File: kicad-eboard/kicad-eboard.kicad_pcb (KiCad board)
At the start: 2 copper layers, 91 parts, among them J1 Conn_01x02, J19 Conn_01x10, SW10 AMT10_Encoder, SW4 LIMIT_1, SW5 LIMIT_2, SW6 AMT10_Encoder, SW7 AMT10_Encoder, SW8 AMT10_Encoder, SW9 AMT10_Encoder, U1 TinkerBoard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

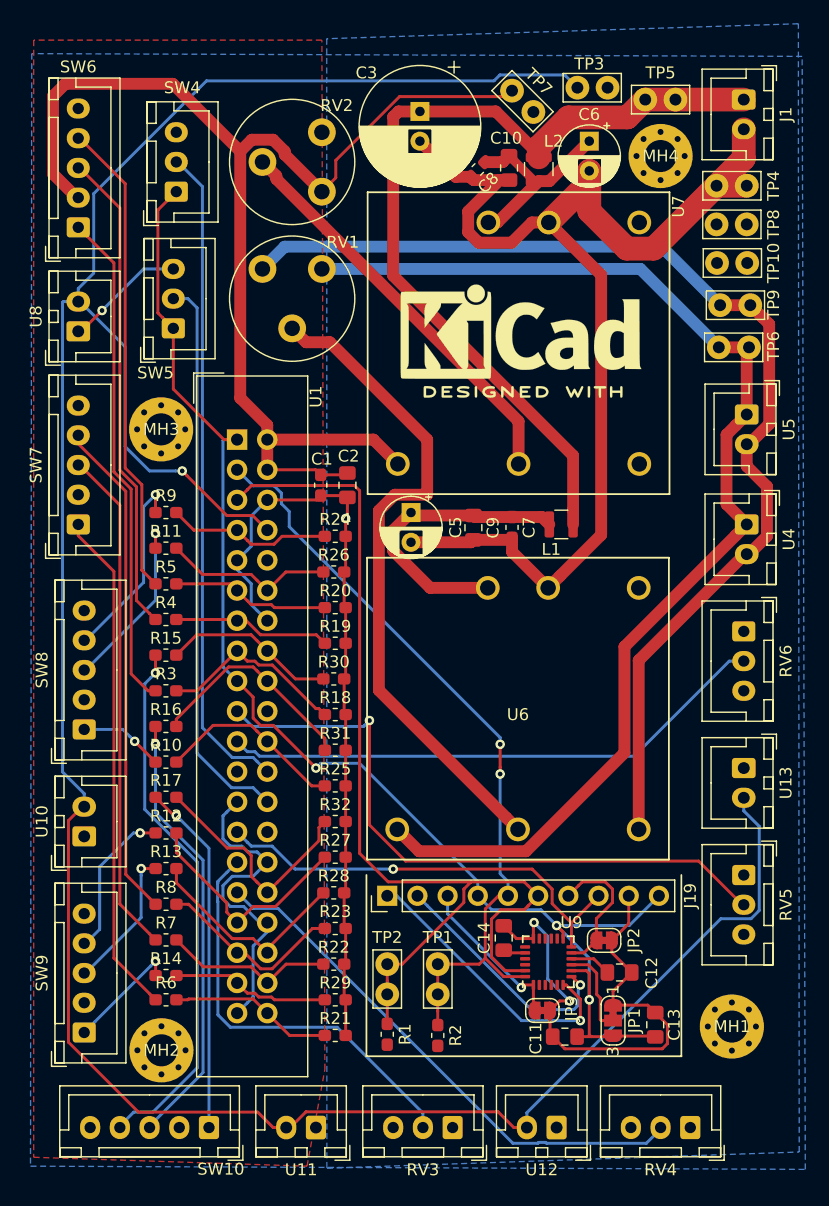
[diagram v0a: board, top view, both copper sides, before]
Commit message: Fix broken 3v3 pour
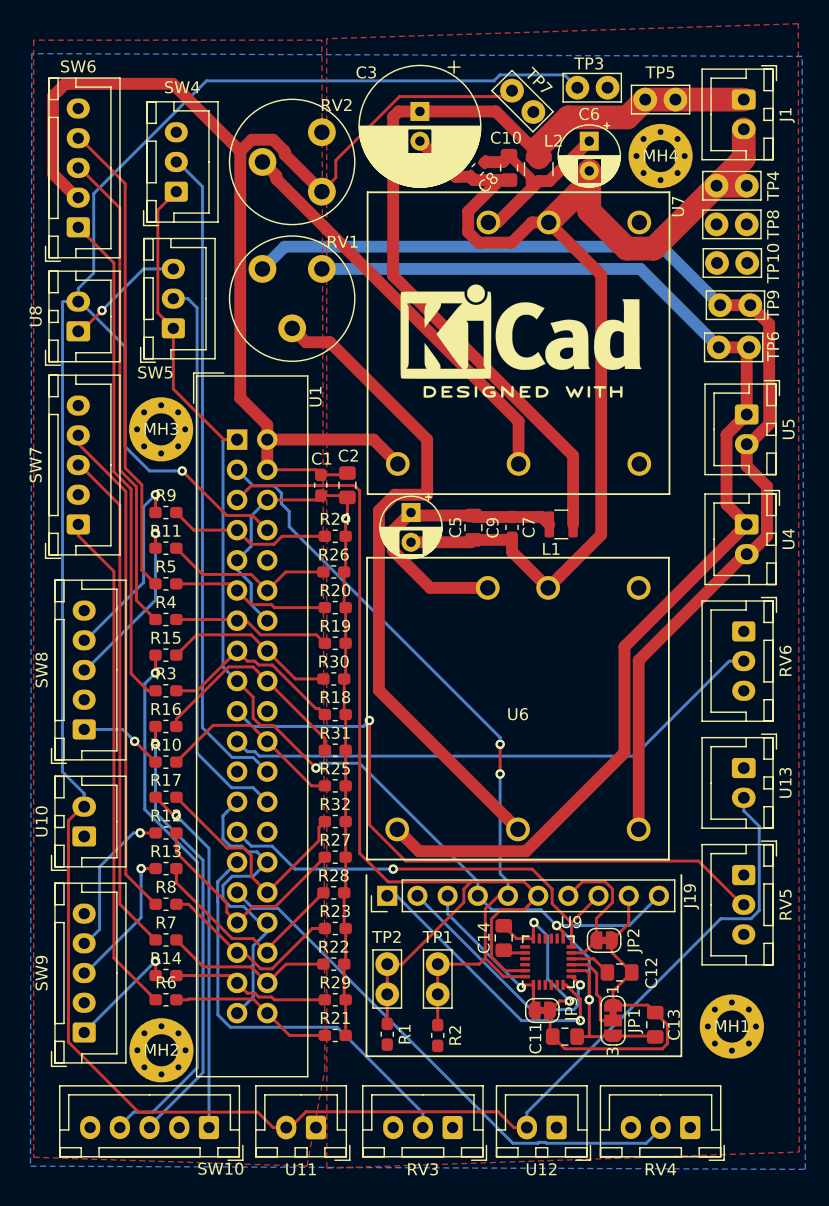
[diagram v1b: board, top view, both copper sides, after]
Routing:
- added copper zone on F.Cu, net +3V3
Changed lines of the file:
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@@
     (add_net "Net-(SW5-Pad2)")
     (add_net "Net-(TP3-Pad1)")
-    (add_net "Net-(U1-Pad10)")
-    (add_net "Net-(U1-Pad23)")
-    (add_net "Net-(U1-Pad28)")
   )
   (module Symbol:KiCad-Logo2_8mm_SilkScreen (layer F.Cu)
@@
   (segment (start 34.101398 84.648602) (end 32.2164 84.648602) (width 0.25) (layer F.Cu) (net 25))
   (segment (start 38.25 80.5) (end 34.101398 84.648602) (width 0.25) (layer F.Cu) (net 25))
-  (segment (start 32.053602 56.708602) (end 32.541402 57.196402) (width 0.25) (layer F.Cu) (net 29))
-  (segment (start 27.958602 56.708602) (end 32.053602 56.708602) (width 0.25) (layer F.Cu) (net 29))
-  (segment (start 32.541402 57.196402) (end 33.405001 58.060001) (width 0.25) (layer F.Cu) (net 29))
-  (segment (start 25.75 54.5) (end 27.958602 56.708602) (width 0.25) (layer F.Cu) (net 29))
-  (segment (start 34.965002 56.5) (end 33.405001 58.060001) (width 0.25) (layer F.Cu) (net 29))
-  (segment (start 38.125 56.5) (end 34.965002 56.5) (width 0.25) (layer F.Cu) (net 29))
   (segment (start 32.541402 69.896402) (end 33.405001 70.760001) (width 0.25) (layer F.Cu) (net 26))
   (segment (start 32.053602 69.408602) (end 32.541402 69.896402) (width 0.25) (layer F.Cu) (net 26))
@@
   (segment (start 18 69.75) (end 21.25 69.75) (width 0.25) (layer B.Cu) (net 28))
   (segment (start 24 72.5) (end 22.25 70.75) (width 0.25) (layer F.Cu) (net 28))
+  (segment (start 32.053602 56.708602) (end 32.541402 57.196402) (width 0.25) (layer F.Cu) (net 29))
+  (segment (start 27.958602 56.708602) (end 32.053602 56.708602) (width 0.25) (layer F.Cu) (net 29))
+  (segment (start 32.541402 57.196402) (end 33.405001 58.060001) (width 0.25) (layer F.Cu) (net 29))
+  (segment (start 25.75 54.5) (end 27.958602 56.708602) (width 0.25) (layer F.Cu) (net 29))
+  (segment (start 34.965002 56.5) (end 33.405001 58.060001) (width 0.25) (layer F.Cu) (net 29))
+  (segment (start 38.125 56.5) (end 34.965002 56.5) (width 0.25) (layer F.Cu) (net 29))
   (segment (start 27.230001 52.980001) (end 25.75 51.5) (width 0.25) (layer F.Cu) (net 30))
   (segment (start 30.865001 52.980001) (end 27.230001 52.980001) (width 0.25) (layer F.Cu) (net 30))
@@
   (segment (start 17.5 45) (end 17.5 45.713285) (width 0.25) (layer F.Cu) (net 32))
   (segment (start 17.5 45.713285) (end 21.5 49.713285) (width 0.25) (layer F.Cu) (net 32))
-  (segment (start 26.785 84.46) (end 30.865001 88.540001) (width 0.25) (layer F.Cu) (net 37))
-  (segment (start 25.76 84.46) (end 26.785 84.46) (width 0.25) (layer F.Cu) (net 37))
-  (segment (start 33.812732 89.8914) (end 32.85281 89.8914) (width 0.25) (layer F.Cu) (net 37))
-  (segment (start 32.85281 89.8914) (end 31.501411 88.540001) (width 0.25) (layer F.Cu) (net 37))
-  (segment (start 37.204132 86.5) (end 33.812732 89.8914) (width 0.25) (layer F.Cu) (net 37))
-  (segment (start 31.501411 88.540001) (end 30.865001 88.540001) (width 0.25) (layer F.Cu) (net 37))
-  (segment (start 38.25 86.5) (end 37.204132 86.5) (width 0.25) (layer F.Cu) (net 37))
-  (segment (start 32.053602 89.728602) (end 32.541402 90.216402) (width 0.25) (layer F.Cu) (net 34))
-  (segment (start 32.541402 90.216402) (end 33.405001 91.080001) (width 0.25) (layer F.Cu) (net 34))
-  (segment (start 28.028602 89.728602) (end 32.053602 89.728602) (width 0.25) (layer F.Cu) (net 34))
-  (segment (start 25.76 87.46) (end 28.028602 89.728602) (width 0.25) (layer F.Cu) (net 34))
-  (segment (start 34.985002 89.5) (end 33.405001 91.080001) (width 0.25) (layer F.Cu) (net 34))
-  (segment (start 38.125 89.5) (end 34.985002 89.5) (width 0.25) (layer F.Cu) (net 34))
   (segment (start 35.285 95.5) (end 33.405001 93.620001) (width 0.25) (layer F.Cu) (net 33))
   (segment (start 38.25 95.5) (end 35.285 95.5) (width 0.25) (layer F.Cu) (net 33))
@@
   (segment (start 33.405001 93.620001) (end 32.2164 92.4314) (width 0.25) (layer F.Cu) (net 33))
   (segment (start 32.2164 92.4314) (end 26.7886 92.4314) (width 0.25) (layer F.Cu) (net 33))
+  (segment (start 32.053602 89.728602) (end 32.541402 90.216402) (width 0.25) (layer F.Cu) (net 34))
+  (segment (start 32.541402 90.216402) (end 33.405001 91.080001) (width 0.25) (layer F.Cu) (net 34))
+  (segment (start 28.028602 89.728602) (end 32.053602 89.728602) (width 0.25) (layer F.Cu) (net 34))
+  (segment (start 25.76 87.46) (end 28.028602 89.728602) (width 0.25) (layer F.Cu) (net 34))
+  (segment (start 34.985002 89.5) (end 33.405001 91.080001) (width 0.25) (layer F.Cu) (net 34))
+  (segment (start 38.125 89.5) (end 34.985002 89.5) (width 0.25) (layer F.Cu) (net 34))
   (segment (start 23.510928 86.960928) (end 24.01 87.46) (width 0.25) (layer F.Cu) (net 35))
   (segment (start 21 84.45) (end 23.510928 86.960928) (width 0.25) (layer F.Cu) (net 35))
@@
   (segment (start 17.5 52.5) (end 17.5 53.45) (width 0.25) (layer F.Cu) (net 36))
   (segment (start 17.5 53.45) (end 20.5 56.45) (width 0.25) (layer F.Cu) (net 36))
-  (segment (start 30.305 57.5) (end 30.865001 58.060001) (width 0.25) (layer F.Cu) (net 42))
-  (segment (start 25.75 57.5) (end 30.305 57.5) (width 0.25) (layer F.Cu) (net 42))
-  (segment (start 31.7286 58.9236) (end 30.865001 58.060001) (width 0.25) (layer F.Cu) (net 42))
-  (segment (start 32.053602 59.248602) (end 31.7286 58.9236) (width 0.25) (layer F.Cu) (net 42))
-  (segment (start 33.748602 59.248602) (end 32.053602 59.248602) (width 0.25) (layer F.Cu) (net 42))
-  (segment (start 34 59.5) (end 33.748602 59.248602) (width 0.25) (layer F.Cu) (net 42))
-  (segment (start 38.25 59.5) (end 34 59.5) (width 0.25) (layer F.Cu) (net 42))
-  (segment (start 30.765 60.5) (end 30.865001 60.600001) (width 0.25) (layer F.Cu) (net 41))
-  (segment (start 25.75 60.5) (end 30.765 60.5) (width 0.25) (layer F.Cu) (net 41))
-  (segment (start 31.645871 60.600001) (end 30.865001 60.600001) (width 0.25) (layer F.Cu) (net 41))
-  (segment (start 32.834472 61.788602) (end 31.645871 60.600001) (width 0.25) (layer F.Cu) (net 41))
-  (segment (start 37.538602 61.788602) (end 32.834472 61.788602) (width 0.25) (layer F.Cu) (net 41))
-  (segment (start 38.25 62.5) (end 37.538602 61.788602) (width 0.25) (layer F.Cu) (net 41))
+  (segment (start 26.785 84.46) (end 30.865001 88.540001) (width 0.25) (layer F.Cu) (net 37))
+  (segment (start 25.76 84.46) (end 26.785 84.46) (width 0.25) (layer F.Cu) (net 37))
+  (segment (start 33.812732 89.8914) (end 32.85281 89.8914) (width 0.25) (layer F.Cu) (net 37))
+  (segment (start 32.85281 89.8914) (end 31.501411 88.540001) (width 0.25) (layer F.Cu) (net 37))
+  (segment (start 37.204132 86.5) (end 33.812732 89.8914) (width 0.25) (layer F.Cu) (net 37))
+  (segment (start 31.501411 88.540001) (end 30.865001 88.540001) (width 0.25) (layer F.Cu) (net 37))
+  (segment (start 38.25 86.5) (end 37.204132 86.5) (width 0.25) (layer F.Cu) (net 37))
   (segment (start 27.505002 66.5) (end 30.865001 63.140001) (width 0.25) (layer F.Cu) (net 38))
   (segment (start 25.75 66.5) (end 27.505002 66.5) (width 0.25) (layer F.Cu) (net 38))
@@
   (segment (start 20.999989 47.940452) (end 22.400022 49.340485) (width 0.25) (layer F.Cu) (net 40))
   (segment (start 17.5 22.5) (end 17.625 22.5) (width 0.25) (layer F.Cu) (net 40))
+  (segment (start 30.765 60.5) (end 30.865001 60.600001) (width 0.25) (layer F.Cu) (net 41))
+  (segment (start 25.75 60.5) (end 30.765 60.5) (width 0.25) (layer F.Cu) (net 41))
+  (segment (start 31.645871 60.600001) (end 30.865001 60.600001) (width 0.25) (layer F.Cu) (net 41))
+  (segment (start 32.834472 61.788602) (end 31.645871 60.600001) (width 0.25) (layer F.Cu) (net 41))
+  (segment (start 37.538602 61.788602) (end 32.834472 61.788602) (width 0.25) (layer F.Cu) (net 41))
+  (segment (start 38.25 62.5) (end 37.538602 61.788602) (width 0.25) (layer F.Cu) (net 41))
+  (segment (start 30.305 57.5) (end 30.865001 58.060001) (width 0.25) (layer F.Cu) (net 42))
+  (segment (start 25.75 57.5) (end 30.305 57.5) (width 0.25) (layer F.Cu) (net 42))
+  (segment (start 31.7286 58.9236) (end 30.865001 58.060001) (width 0.25) (layer F.Cu) (net 42))
+  (segment (start 32.053602 59.248602) (end 31.7286 58.9236) (width 0.25) (layer F.Cu) (net 42))
+  (segment (start 33.748602 59.248602) (end 32.053602 59.248602) (width 0.25) (layer F.Cu) (net 42))
+  (segment (start 34 59.5) (end 33.748602 59.248602) (width 0.25) (layer F.Cu) (net 42))
+  (segment (start 38.25 59.5) (end 34 59.5) (width 0.25) (layer F.Cu) (net 42))
   (segment (start 20.5 48.076874) (end 21.950011 49.526885) (width 0.25) (layer F.Cu) (net 43))
   (segment (start 21.950011 65.075011) (end 23.375 66.5) (width 0.25) (layer F.Cu) (net 43))
@@
     )
   )
-  (zone (net 7) (net_name GND) (layer B.Cu) (hatch edge 0.508)
+  (zone (net 9) (net_name +3V3) (layer F.Cu) (hatch edge 0.508)
     (connect_pads (clearance 0.508))
     (min_thickness 0.254)

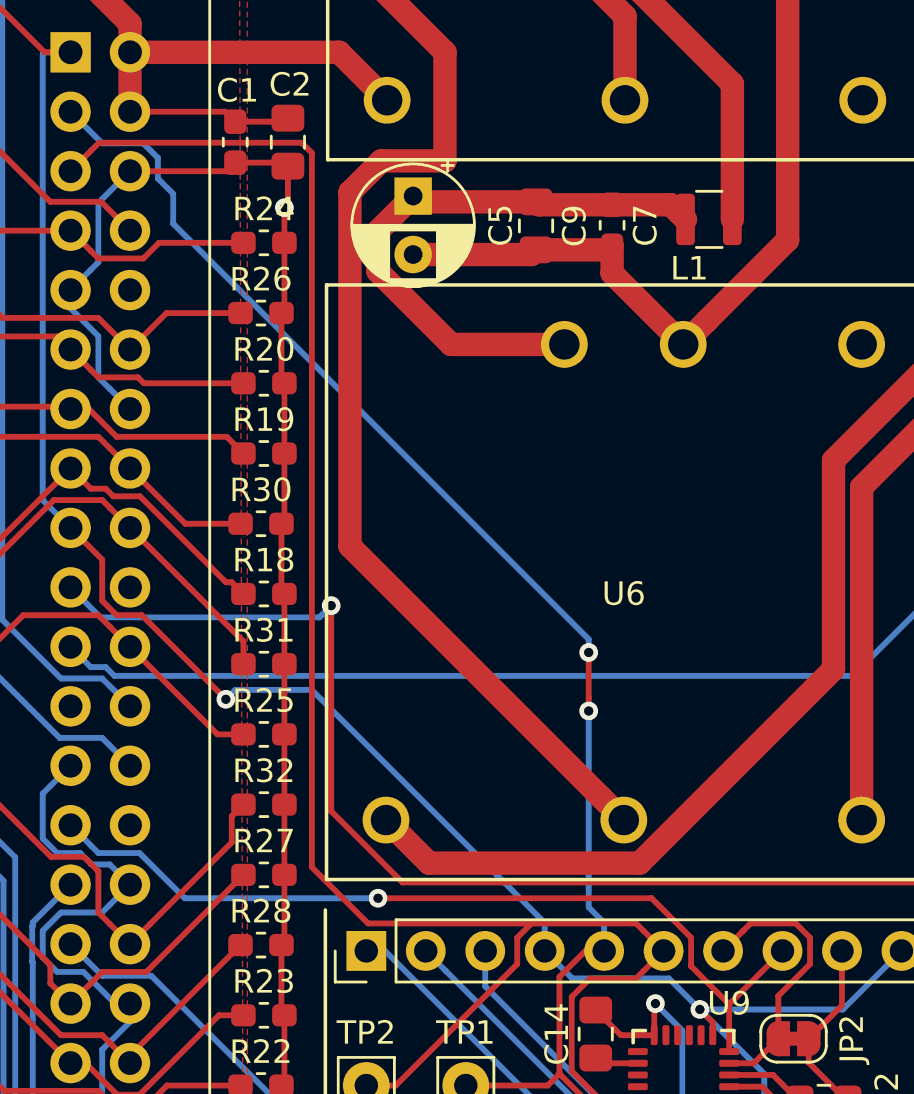
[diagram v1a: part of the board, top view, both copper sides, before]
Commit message: Add SSH logo; move vias to accomodate
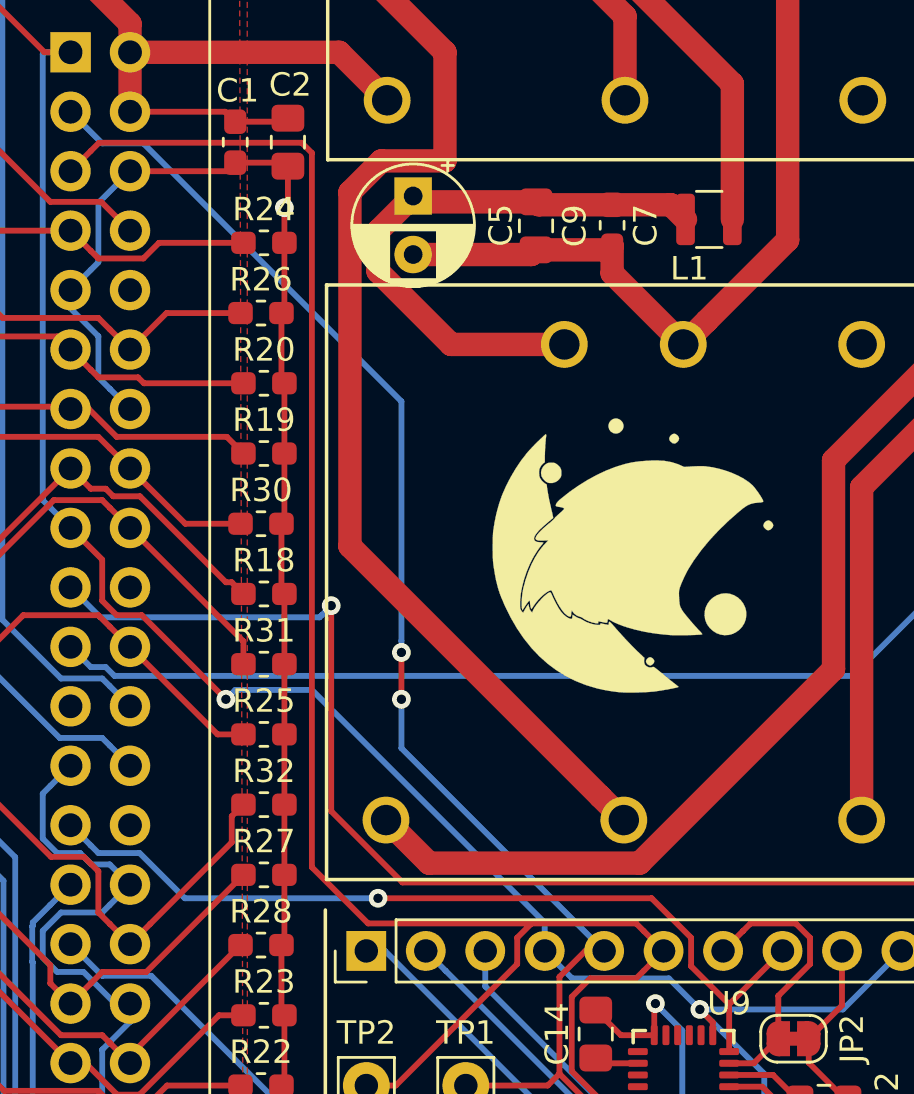
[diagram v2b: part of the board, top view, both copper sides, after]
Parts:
- added G2: LOGO, 2019Spacehawks:SSH_logo, F.Cu at (55.0, 66.5)
- renumbered REF** to G1

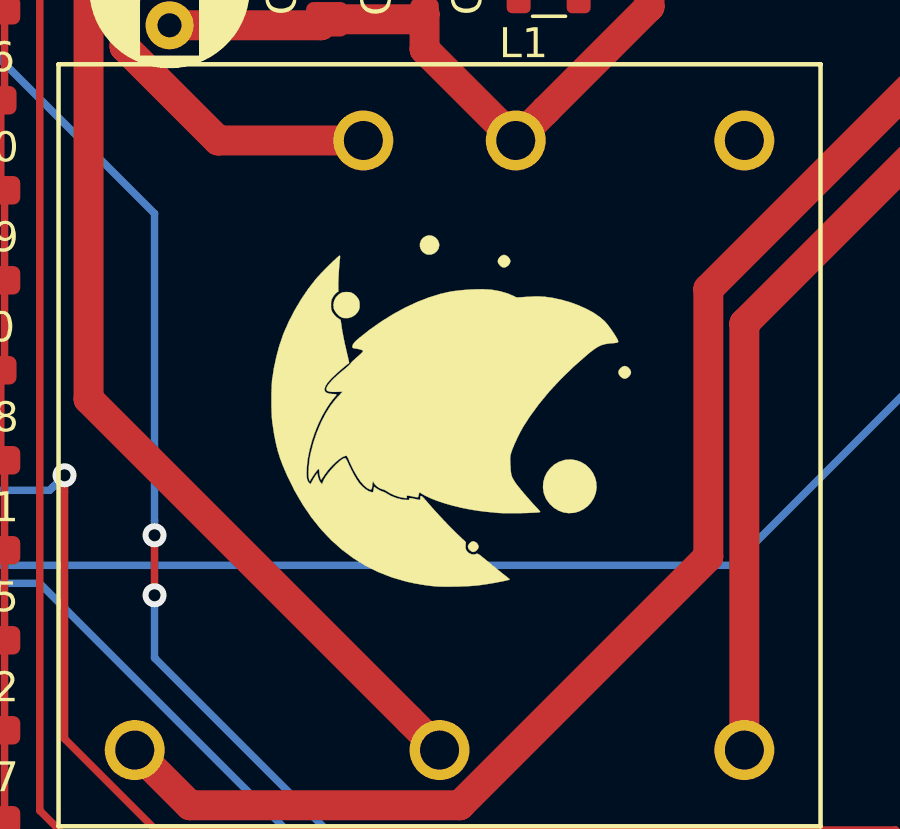
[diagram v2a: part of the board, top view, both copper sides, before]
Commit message: Tweak logo
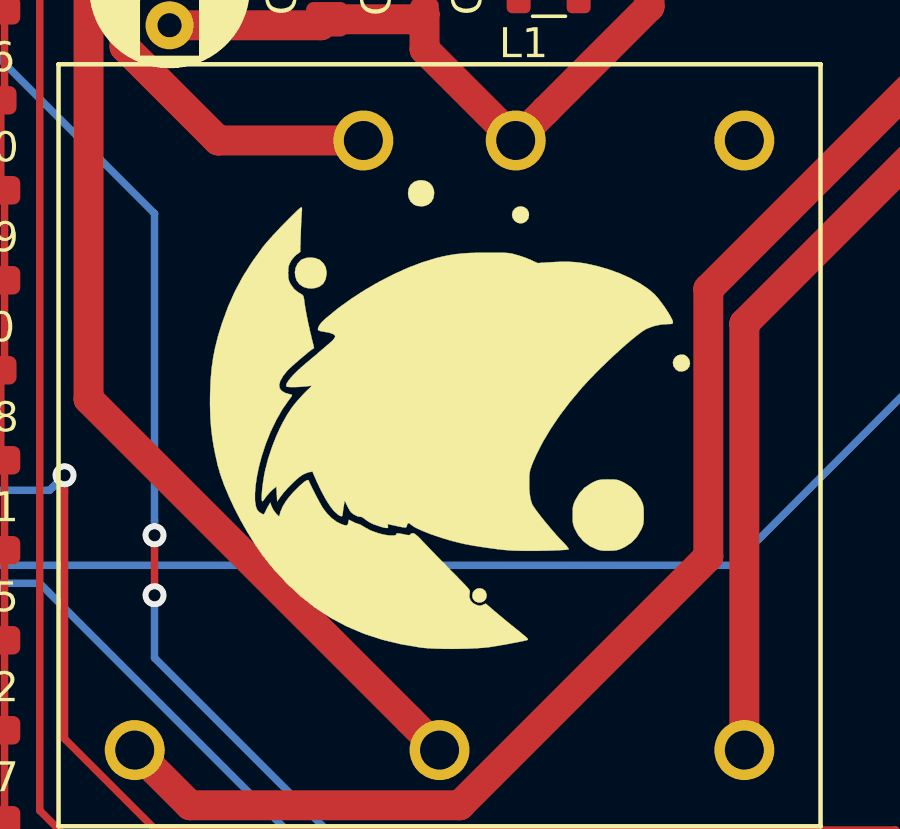
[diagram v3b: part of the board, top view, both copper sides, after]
